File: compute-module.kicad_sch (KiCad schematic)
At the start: 13 parts, among them J7 DF40HC(3.0)-100DS-0.4v, J8 DF40HC(3.0)-100DS-0.4v, M1 compute-module-4-1.5mm, Q6 BSS138-7-F

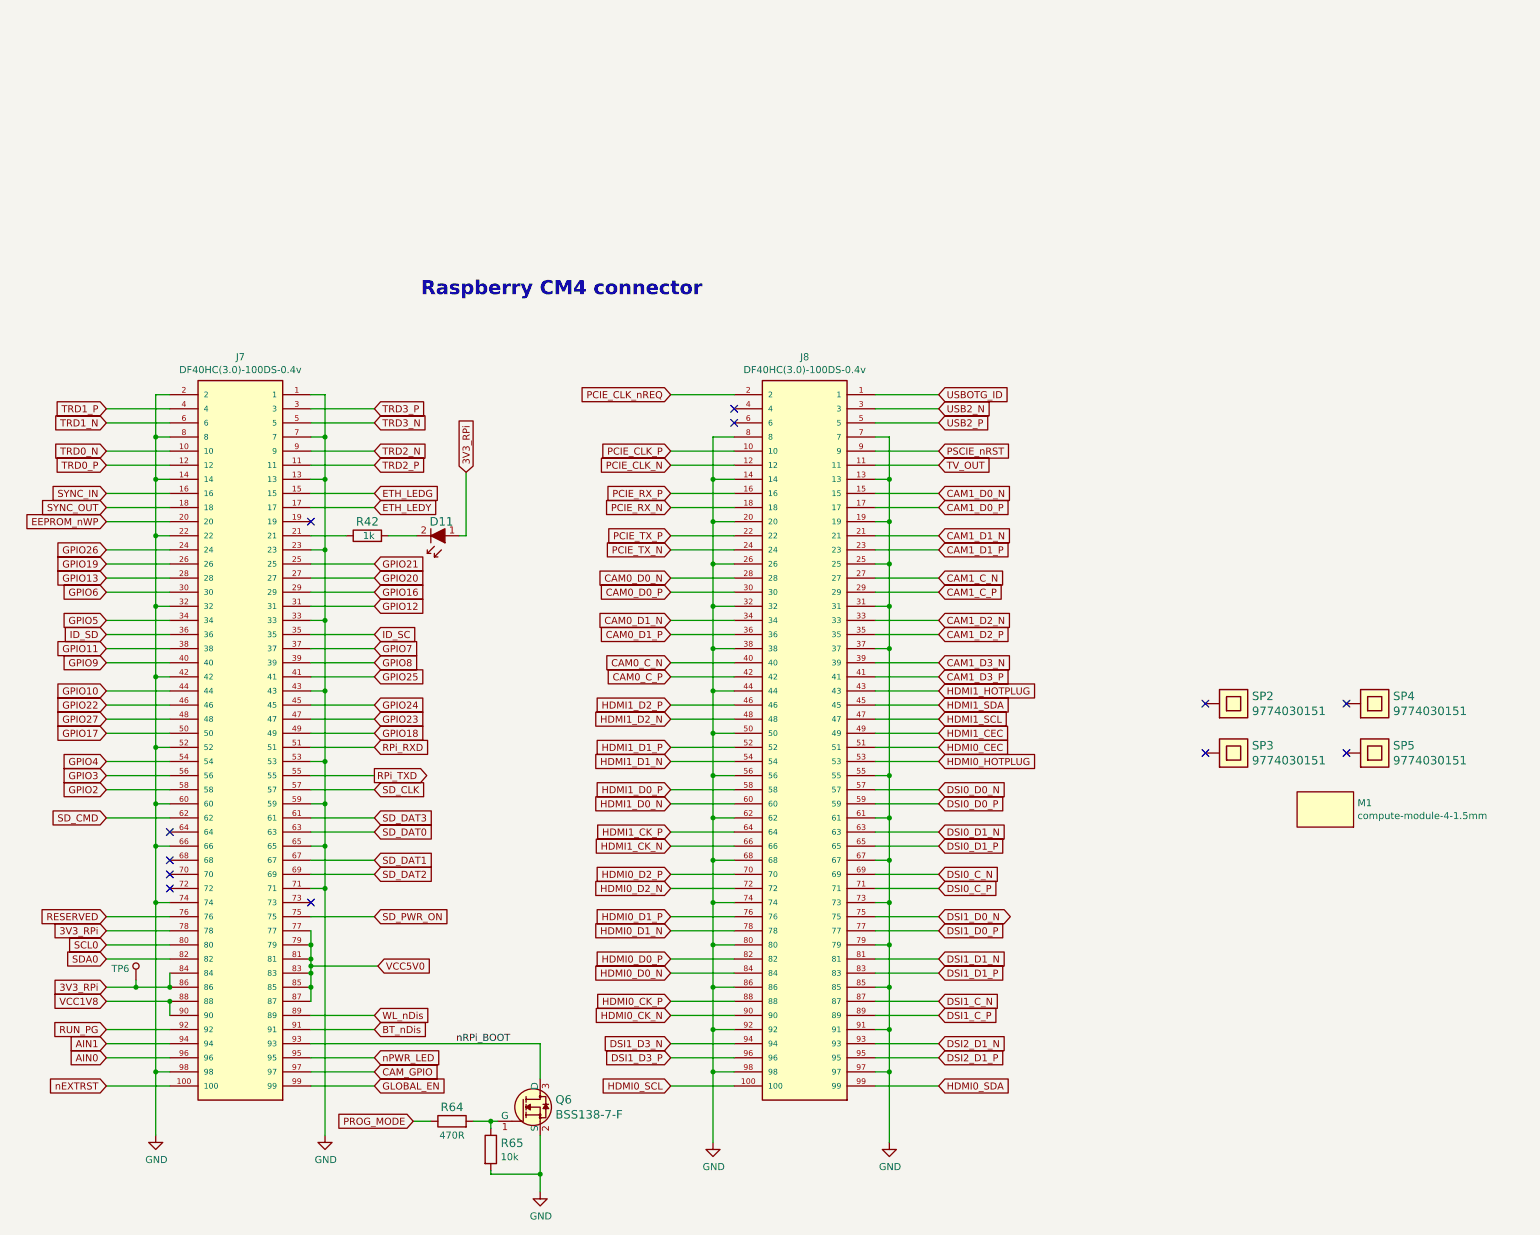
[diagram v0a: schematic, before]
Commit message: Update DF40HC(3.0)-100DS-0.4v symbol and footprint
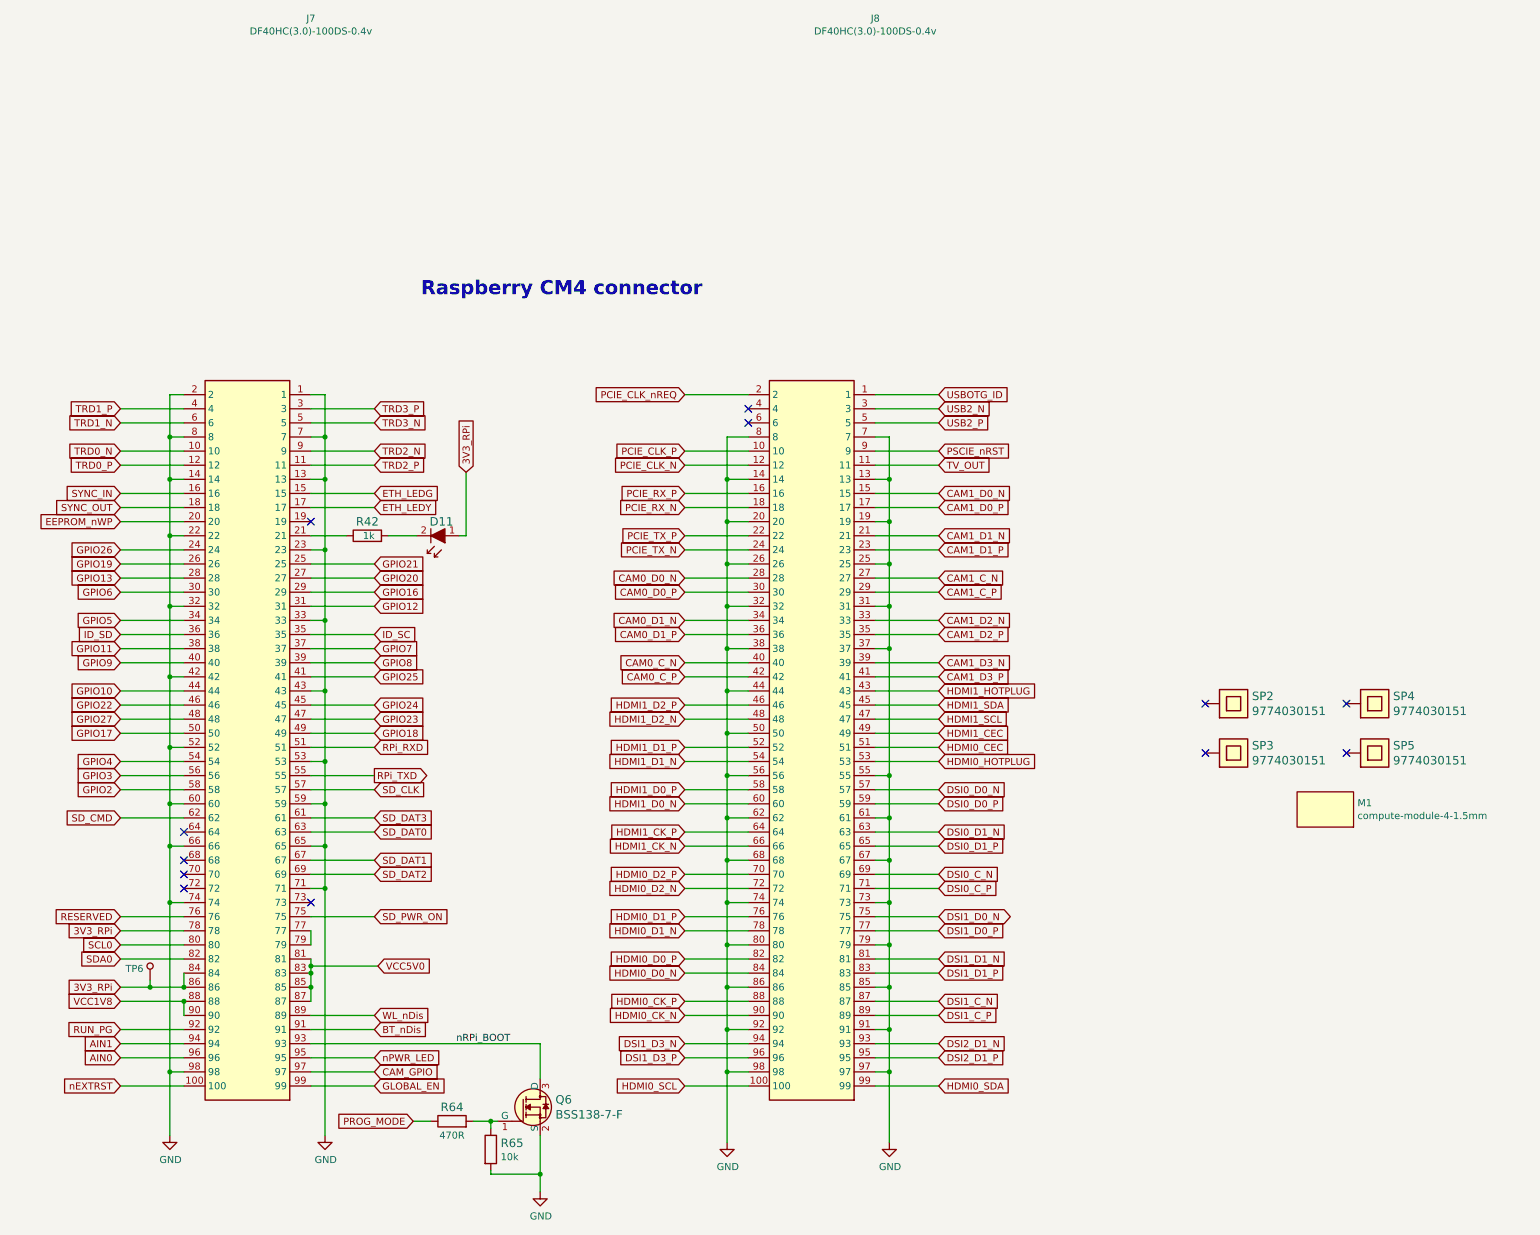
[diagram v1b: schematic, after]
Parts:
- J7, J8: footprint scalenode-cm4-baseboard-footprints:DF40HC(3.0)-100DS-0.4v -> antmicro-footprints:DF40HC(3.0)-100DS-0.4v; symbol scalenode-cm4-baseboard:DF40HC(3.0)-100DS-0.4v -> antmicroRectangularConnectorsHeadersMalePins:DF40HC(3.0)-100DS-0.4v; Author (none) -> Antmicro; Copyright (none) -> Copyright (c) 2023 Antmicro; License (none) -> Apache-2.0; Manufacturer HRS -> Hirose
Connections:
- net VCC5V0: no longer J7.77, J7.79
- new net: J7.77, J7.79
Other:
- moved on the sheet: J7, J8, TP6

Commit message: Delete copyright field
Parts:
- J7, J8: Copyright Copyright (c) 2023 Antmicro -> (none)

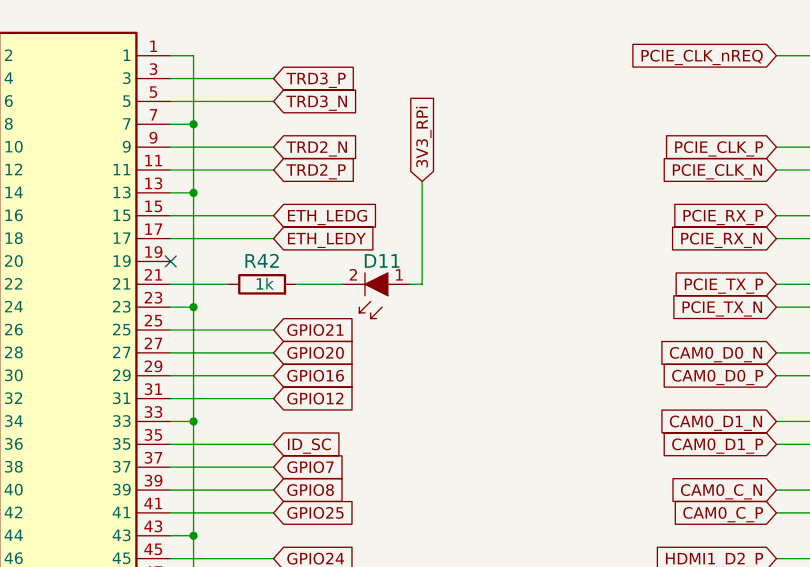
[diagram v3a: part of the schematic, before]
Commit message: Update D1, D11 symbol
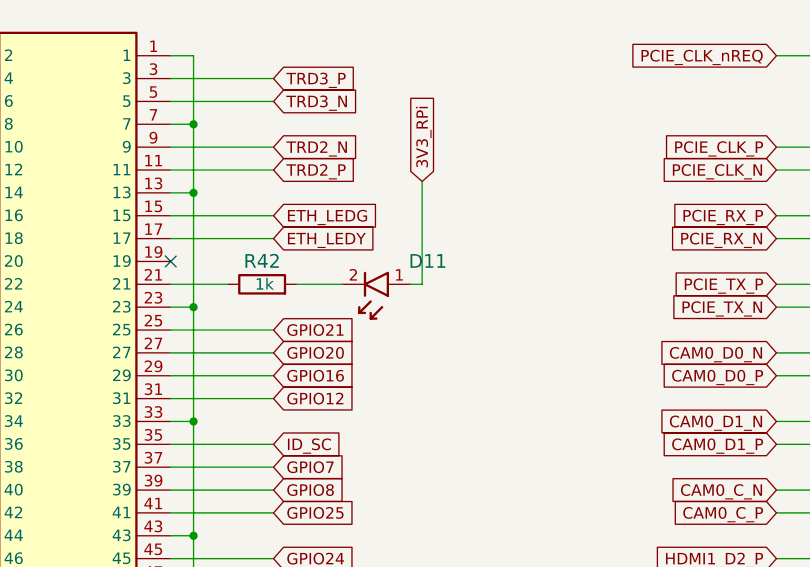
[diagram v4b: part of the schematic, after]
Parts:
- D11: footprint scalenode-cm4-baseboard-footprints:LED_0603_R -> antmicro-footprints:LED_0603_1608Metric_R; symbol scalenode-cm4-baseboard:598-8D80-107F -> antmicroLEDIndicationDiscrete:598-8D80-107F; Author (none) -> Antmicro; License (none) -> Apache-2.0

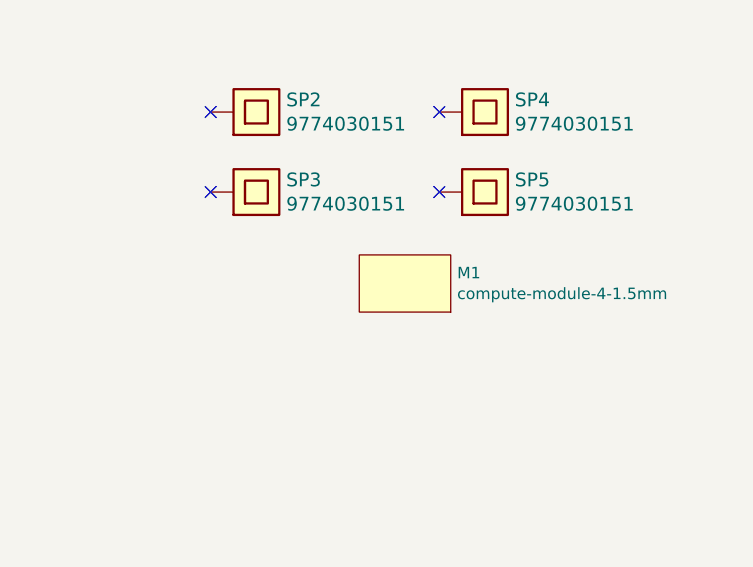
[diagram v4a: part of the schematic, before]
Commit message: Update M1 symbol and footprint
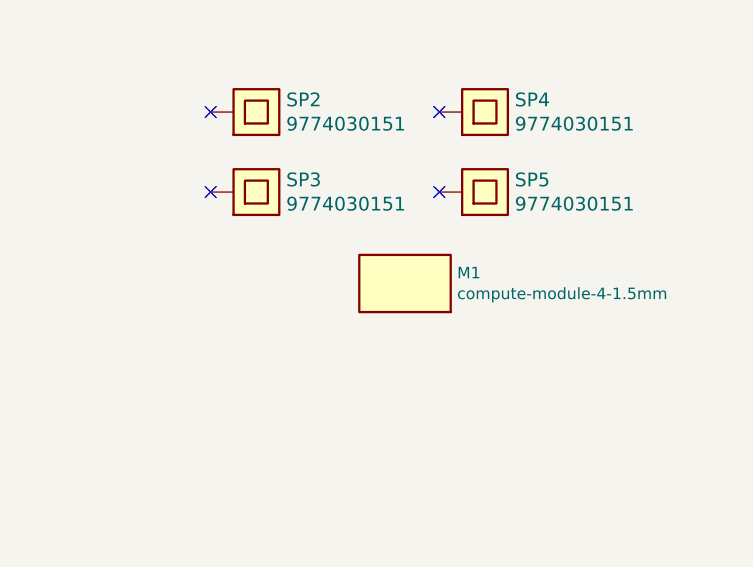
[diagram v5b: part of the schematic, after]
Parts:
- M1: footprint scalenode-cm4-baseboard-footprints:compute-module-4-1.5mm -> antmicro-footprints:compute-module-4-1.5mm; symbol scalenode-cm4-baseboard:compute-module-4-1.5mm -> antmicroModules:compute-module-4-1.5mm; Author (none) -> Antmicro; License (none) -> Apache-2.0; MPN (none) -> SC0294; Manufacturer (none) -> Raspberry Pi

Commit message: Update D1, D11 symbol
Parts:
- D11: symbol antmicroLEDIndicationDiscrete:598-8D80-107F -> antmicroLEDIndicationDiscrete:LED_R_0603_598-8D80-107F
